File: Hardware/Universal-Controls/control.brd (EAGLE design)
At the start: 32.7 x 46.2 mm, 44 parts, among them U1 STM32-M-64-LQFP, U2 MIC5233-5.0YM5-TR, U3 MIC5233-3.3YM5-TR, U4 TJA1042HVSON, U6 MCP6002, Y1 16MHz

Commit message: Button controller commit
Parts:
- removed C26: 100nF, comma.ai:0603-C
- removed R1, R2, R3, R4, R7, R8: 10k, comma.ai:0402-R
- removed R23, R24, R25, R26: 1k, comma.ai:0402-R
- removed U$1: MICROFIT-6, interceptor:MICROFIT-6
- removed U6: MCP6002, comma.ai:SO08
- moved C8 26.7 mm to (8.18, 46.2), flipped to the bottom, turned to 180 degrees
- moved C2 22.2 mm to (13.2, 41.0), flipped to the bottom, turned to 270 degrees
- moved U$3 22.1 mm to (12.0, 29.9), turned to 270 degrees
- moved R13 21.1 mm to (13.9, 36.4)
- moved LED1 20.7 mm to (15.6, 36.0), turned to 0 degrees
- moved C1 18.5 mm to (14.7, 46.2)
- moved C14 17.7 mm to (27.7, 37.2), flipped to the bottom, turned to 180 degrees
- moved C11 17.5 mm to (15.3, 40.9), turned to 90 degrees
- moved S1 17.5 mm to (19.8, 27.6), turned to 270 degrees
- moved C10 17.3 mm to (14.7, 48.3)
- moved C9 17.1 mm to (8.13, 48.2)
- moved C12 17.1 mm to (8.28, 40.4)
- moved C13 17.1 mm to (8.23, 42.4)
- moved U1 17.0 mm to (11.4, 44.3)
- moved S2 16.8 mm to (15.9, 27.6), turned to 270 degrees
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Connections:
- removed net ACCEL1: R23.2, U$3.2
- removed net ACCEL2: R24.2, U$3.5
- removed net DAC1: R3.2, U$1.2, U6.1
- removed net DAC2: R2.2, U$1.5, U6.7
- removed net DACV: C26.1, U$1.3, U$1.6, U6.8
- removed net N$17: R7.2, U1.20, U6.3
- removed net N$18: R8.2, U1.21, U6.5
- removed net N$21: R1.2, R3.1, U6.2
- removed net N$22: R2.1, R4.2, U6.6
- removed net N$41: R23.1, R26.1, U1.8
- removed net N$42: R24.1, R25.1, U1.9
- new net ADC: U$3.2, U1.8
- new net ENC1: U$3.4, U1.41
- new net ENC2: U$3.5, U1.42
- new net IO1: U$3.6, U1.43
- net 3V3: now also U$3.3
- net 5V: no longer U$3.3, U$3.6
- net GND: no longer C26.2, R1.1, R25.2, R26.2, R4.1, R7.1, R8.1, U$1.1, U$1.4, U$3.4, U6.4
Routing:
- net N$7: track 8.04 -> 53.5 mm, vias 0 -> 2
- net N$10: track 9.10 -> 46.2 mm, vias 0 -> 2
- net ADC: track 0.00 -> 36.5 mm, vias 0 -> 1
- net 5V: track 69.1 -> 41.0 mm
- net N$42: track 26.5 -> 0.00 mm, vias 1 -> 0
- net ENC1: track 0.00 -> 25.0 mm, vias 0 -> 2
- net N$41: track 24.5 -> 0.00 mm, vias 1 -> 0
- net ENC2: track 0.00 -> 22.0 mm, vias 0 -> 2
- net IO1: track 0.00 -> 19.8 mm, vias 0 -> 2
- net N$4: track 2.72 -> 15.2 mm
- net DAC2: track 12.1 -> 0.00 mm
- net DACV: track 12.1 -> 0.00 mm, vias 1 -> 0
- net N$2: track 3.51 -> 14.2 mm
- net N$18: track 8.44 -> 0.00 mm
- net 12V: track 6.91 -> 14.1 mm
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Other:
- board size 32.7 x 46.2 mm -> 32.7 x 28 mm
- board text added: "B"
- board text added: "R"
- board text removed: "BOOT"
- board text removed: "IN"
- board text removed: "RST"

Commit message: final board prep for manufacture
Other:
- board text added: "3V3 ADC GND IO1 EN2 EN1"
- board text added: "GND CANL CANH 12V"
- board text added: "Ocelot Universal cruise controls"
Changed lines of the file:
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@@
 <text x="18.7" y="32.3" size="1.778" layer="25">R</text>
 <text x="15.2" y="32.2" size="1.778" layer="25">B</text>
+<text x="25" y="40" size="1.4224" layer="25">GND
+CANL
+CANH
+12V</text>
+<text x="0.5" y="34.1" size="1.016" layer="25" rot="SR270">3V3 ADC GND
+IO1  EN2 EN1</text>
+<text x="28.8" y="29.4" size="1.016" layer="26" rot="MR0">Ocelot
+Universal cruise controls</text>
 </plain>
 <attributes>
@@
 </element>
 <element name="C14" library="rcl" library_urn="urn:adsk.eagle:library:334" package="C0603" package3d_urn="urn:adsk.eagle:package:23616/2" value="2.2u" x="27.71" y="37.17" smashed="yes" rot="MR180">
-<attribute name="NAME" x="28.665" y="38.475" size="1.27" layer="26" rot="MR90"/>
+<attribute name="NAME" x="29.275" y="37.635" size="1.27" layer="26" rot="MR180"/>
 <attribute name="POPULARITY" value="73" x="74.7" y="86.7" size="1.778" layer="28" rot="MR180" display="off"/>
 <attribute name="SPICEPREFIX" value="C" x="74.7" y="86.7" size="1.778" layer="28" rot="MR180" display="off"/>
@@
 </element>
 <element name="D1" library="diode" library_urn="urn:adsk.eagle:library:210" package="SOT23" package3d_urn="urn:adsk.eagle:package:43389/2" value="BAS40" x="30.78" y="31.82" smashed="yes" rot="MR0">
-<attribute name="NAME" x="30.085" y="26.955" size="1.27" layer="26" rot="MR90"/>
+<attribute name="NAME" x="28.385" y="32.855" size="1.27" layer="26" rot="MR90"/>
 <attribute name="POPULARITY" value="0" x="13" y="-11.36" size="1.778" layer="28" rot="MR0" display="off"/>
 </element>
@@
 <attribute name="MOUSER_PART_NUMBER" value="998-MIC5233-5.0YM5TR" x="83.7" y="4.7" size="1.778" layer="28" rot="MR270" display="off"/>
 <attribute name="MOUSER_PRICE-STOCK" value="https://www.mouser.co.uk/ProductDetail/Microchip-Technology-Micrel/MIC5233-50YM5-TR?qs=U6T8BxXiZAWSnpCHgrMajw%3D%3D" x="83.7" y="4.7" size="1.778" layer="28" rot="MR270" display="off"/>
-<attribute name="NAME" x="30.81" y="46.38" size="1.27" layer="26" rot="MR0" align="center"/>
+<attribute name="NAME" x="30.61" y="47.08" size="1.27" layer="26" rot="MR0" align="center"/>
 </element>
 <element name="R10" library="comma.ai" package="0402-R" value="5.1k" x="23.39" y="33.45" smashed="yes" rot="R270">
@@
 </element>
 <element name="R13" library="comma.ai" package="0402-R" value="220" x="13.9" y="36.43" smashed="yes" rot="R270">
-<attribute name="NAME" x="13.135" y="37.662" size="0.6096" layer="25"/>
+<attribute name="NAME" x="13.138" y="35.535" size="0.6096" layer="25" rot="R90"/>
 </element>
 <element name="R16" library="comma.ai" package="0402-R" value="22" x="21" y="33.41" smashed="yes" rot="R270">
@@
 </drawing>
 <compatibility>
+<note version="6.3" minversion="6.2.2" severity="warning">
+Since Version 6.2.2 text objects can contain more than one line,
+which will not be processed correctly with this version.
+</note>
 <note version="8.2" severity="warning">
 Since Version 8.2, EAGLE supports online libraries. The ids

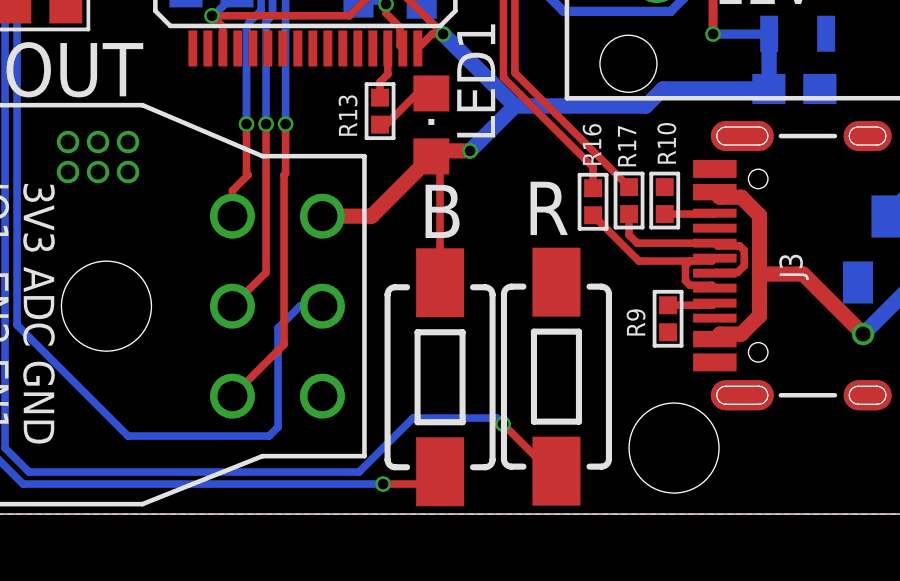
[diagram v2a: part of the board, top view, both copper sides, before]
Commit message: add pull resistors
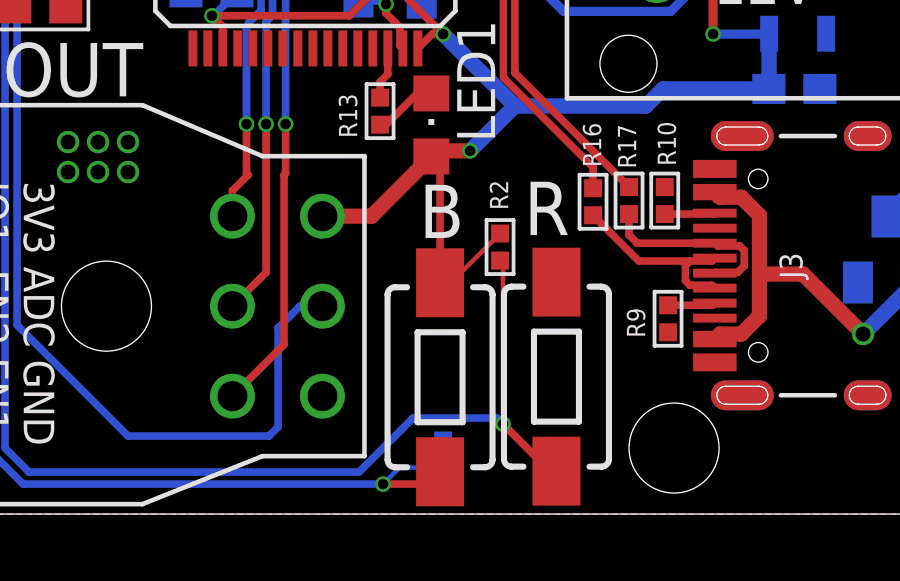
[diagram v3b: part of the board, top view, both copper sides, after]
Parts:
- added R1, R2: (no value), comma.ai:0402-R
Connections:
- net 3V3: now also R2.1
- net GND: now also R1.1
- net N$10: now also R2.2
- net N$7: now also R1.2
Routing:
- net N$10: track 46.2 -> 51.7 mm
- net 3V3: track 79.9 -> 82.6 mm
- net N$7: track 53.5 -> 55.7 mm
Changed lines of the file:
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@@
 <attribute name="NAME" x="4.33" y="44.77" size="0.6096" layer="21" rot="R270"/>
+</element>
+<element name="R1" library="comma.ai" package="0402-R" value="" x="16" y="25" smashed="yes" rot="MR270">
+<attribute name="NAME" x="15.238" y="25.635" size="0.6096" layer="26" rot="MR270"/>
+</element>
+<element name="R2" library="comma.ai" package="0402-R" value="" x="17.9" y="31.9" smashed="yes" rot="R270">
+<attribute name="NAME" x="17.562" y="34.135" size="0.6096" layer="25" rot="R270"/>
 </element>
 </elements>
@@
 <via x="5.5" y="50" extent="1-16" drill="0.5"/>
 <via x="21" y="41.1" extent="1-16" drill="0.5"/>
+<contactref element="R1" pad="1"/>
+<wire x1="28.64" y1="43.47" x2="27.82" y2="47.86" width="0" layer="19" extent="16-16"/>
+<wire x1="27.82" y1="41.51" x2="28.64" y2="43.47" width="0" layer="19" extent="16-16"/>
+<wire x1="28.56" y1="37.17" x2="27.82" y2="41.51" width="0" layer="19" extent="16-16"/>
+<wire x1="30.155" y1="35.6" x2="28.56" y2="37.17" width="0" layer="19" extent="1-16"/>
+<wire x1="25.06" y1="34.505" x2="25.975" y2="35.6" width="0" layer="19" extent="1-16"/>
+<wire x1="25.06" y1="28.055" x2="25.975" y2="26.96" width="0" layer="19" extent="1-1"/>
+<wire x1="23.39" y1="33.9" x2="25.06" y2="34.505" width="0" layer="19" extent="1-1"/>
+<wire x1="23.5" y1="29.06" x2="25.06" y2="28.055" width="0" layer="19" extent="1-1"/>
+<wire x1="19.78" y1="30.73" x2="23.5" y2="29.06" width="0" layer="19" extent="1-1"/>
+<wire x1="23.13" y1="46.86" x2="27.82" y2="47.86" width="0" layer="19" extent="16-16"/>
+<wire x1="19.29" y1="49.02" x2="23.13" y2="46.86" width="0" layer="19" extent="16-16"/>
+<wire x1="18.88" y1="44.47" x2="19.29" y2="49.02" width="0" layer="19" extent="16-16"/>
+<wire x1="19.51" y1="41.71" x2="18.88" y2="44.47" width="0" layer="19" extent="16-16"/>
+<wire x1="21" y1="41.1" x2="21" y2="42" width="0" layer="19" extent="1-1"/>
+<wire x1="15.29" y1="41.76" x2="17.38" y2="44.17" width="0" layer="19" extent="16-16"/>
+<wire x1="13.18" y1="41.8" x2="15.29" y2="41.76" width="0" layer="19" extent="16-16"/>
+<wire x1="11.7" y1="41.7" x2="13.18" y2="41.8" width="0" layer="19" extent="16-16"/>
+<wire x1="9.08" y1="42.41" x2="11.7" y2="41.7" width="0" layer="19" extent="16-16"/>
+<wire x1="8.9" y1="44.3" x2="9.08" y2="42.41" width="0" layer="19" extent="16-16"/>
+<wire x1="9.029" y1="46.159" x2="8.9" y2="44.3" width="0" layer="19" extent="16-16"/>
+<wire x1="8.982" y1="48.217" x2="9.029" y2="46.159" width="0" layer="19" extent="16-16"/>
+<wire x1="8.16" y1="50.02" x2="8.982" y2="48.217" width="0" layer="19" extent="1-16"/>
+<wire x1="7.43" y1="40.39" x2="9.08" y2="42.41" width="0" layer="19" extent="16-16"/>
+<wire x1="8.16" y1="38.52" x2="7.43" y2="40.39" width="0" layer="19" extent="1-16"/>
+<wire x1="5.5" y1="50" x2="8.16" y2="50.02" width="0" layer="19" extent="1-1"/>
+<wire x1="5.66" y1="42.52" x2="7.43" y2="40.39" width="0" layer="19" extent="1-16"/>
+<wire x1="3.43" y1="44.07" x2="5.66" y2="42.52" width="0" layer="19" extent="1-1"/>
+<wire x1="1.69" y1="45.91" x2="3.43" y2="44.07" width="0" layer="19" extent="1-1"/>
+<wire x1="1.73" y1="41.77" x2="3.43" y2="44.07" width="0" layer="19" extent="1-1"/>
+<wire x1="1.727" y1="39.853" x2="1.73" y2="41.77" width="0" layer="19" extent="1-1"/>
+<wire x1="13.16" y1="38.52" x2="13.18" y2="41.8" width="0" layer="19" extent="1-16"/>
+<wire x1="13.81" y1="46.18" x2="17.38" y2="44.17" width="0" layer="19" extent="16-16"/>
+<wire x1="13.85" y1="48.29" x2="13.81" y2="46.18" width="0" layer="19" extent="16-16"/>
+<wire x1="5.5" y1="35.4" x2="8.16" y2="38.52" width="0" layer="19" extent="1-1"/>
+<wire x1="5.5" y1="34.4" x2="5.5" y2="35.4" width="0" layer="19" extent="1-1"/>
+<wire x1="4.5" y1="35.4" x2="5.5" y2="35.4" width="0" layer="19" extent="1-1"/>
+<wire x1="3.5" y1="35.4" x2="4.5" y2="35.4" width="0" layer="19" extent="1-1"/>
+<wire x1="4.5" y1="34.4" x2="5.5" y2="34.4" width="0" layer="19" extent="1-1"/>
+<wire x1="3.5" y1="34.4" x2="3.5" y2="35.4" width="0" layer="19" extent="1-1"/>
+<wire x1="11.98" y1="26.93" x2="19.78" y2="30.73" width="0" layer="19" extent="1-1"/>
+<wire x1="16" y1="25.45" x2="11.98" y2="26.93" width="0" layer="19" extent="16-16"/>
 </signal>
 <signal name="VCAP2">
@@
 <wire x1="15.9" y1="30.71" x2="15.9" y2="34.63" width="0.254" layer="1"/>
 <wire x1="15.9" y1="34.63" x2="15.61" y2="34.92" width="0.254" layer="1"/>
+<contactref element="R2" pad="1"/>
+<wire x1="17.9" y1="32.35" x2="16.26" y2="30.71" width="0.1524" layer="1"/>
+<wire x1="16.26" y1="30.71" x2="15.9" y2="30.71" width="0.1524" layer="1"/>
 </signal>
 <signal name="N$1">
@@
 <wire x1="18" y1="26" x2="19.57" y2="24.43" width="0.254" layer="1"/>
 <wire x1="19.57" y1="24.43" x2="19.78" y2="24.43" width="0.254" layer="1"/>
+<contactref element="R2" pad="2"/>
+<wire x1="17.9" y1="31.45" x2="18" y2="31.35" width="0.1524" layer="1"/>
+<wire x1="18" y1="31.35" x2="18" y2="26" width="0.1524" layer="1"/>
 </signal>
 <signal name="N$7">
@@
 <wire x1="1" y1="45" x2="2.9698" y2="46.9698" width="0.254" layer="16"/>
 <wire x1="11.26955625" y1="49" x2="10.0707875" y2="49" width="0.254" layer="1"/>
+<contactref element="R1" pad="2"/>
+<wire x1="14" y1="24" x2="14.55" y2="24.55" width="0.1524" layer="16"/>
+<wire x1="14.55" y1="24.55" x2="16" y2="24.55" width="0.1524" layer="16"/>
 </signal>
 <signal name="N$11">
